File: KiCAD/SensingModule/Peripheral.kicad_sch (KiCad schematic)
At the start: 8 parts, among them J3 TERMISTOR, U10 BME280, U5 MB85RS2MT, U6 MB85RS2MT, U7 MB85RS2MT, U8 MB85RS2MT, U9 BNO055

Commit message: 配線作業終了、確認お願いします
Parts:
- J3: footprint TSRP_Connector_Hirose:DF51-2P-2DS -> TSRP_Connector:DF1B-2S-2.5R
- U9: footprint Akizuki_BNO055_Module:BNO055 -> TSRP_IC:AE-BNO055-BO
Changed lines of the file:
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@@
 			)
 		)
-		(property "Footprint" "Akizuki_BNO055_Module:BNO055"
+		(property "Footprint" "TSRP_IC:AE-BNO055-BO"
 			(at 179.07 41.91 0)
 			(effects
@@
 			)
 		)
-		(property "Footprint" "TSRP_Connector_Hirose:DF51-2P-2DS"
+		(property "Footprint" "TSRP_Connector:DF1B-2S-2.5R"
 			(at 105.41 46.99 0)
 			(effects

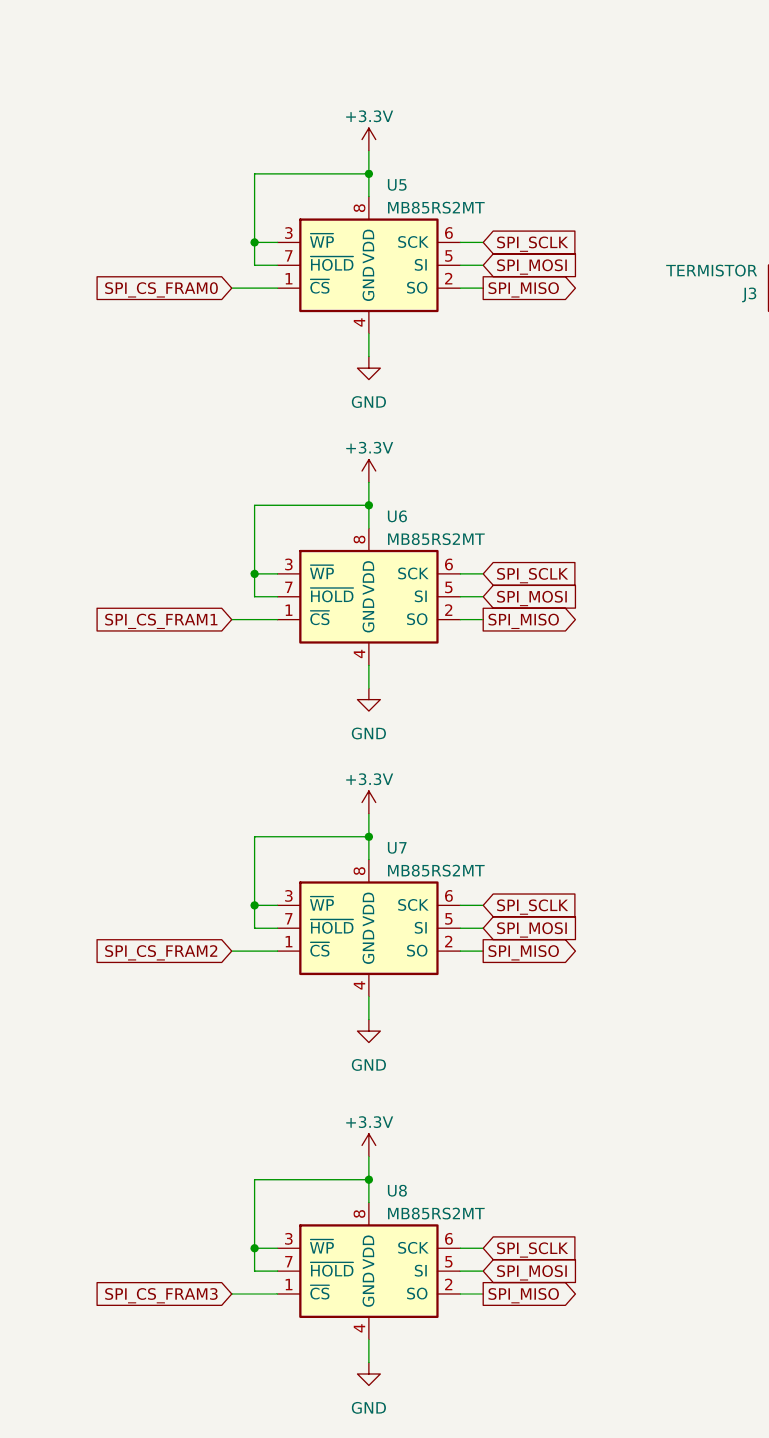
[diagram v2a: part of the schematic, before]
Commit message: Sensingの配線作業終わり、確認お願いします。
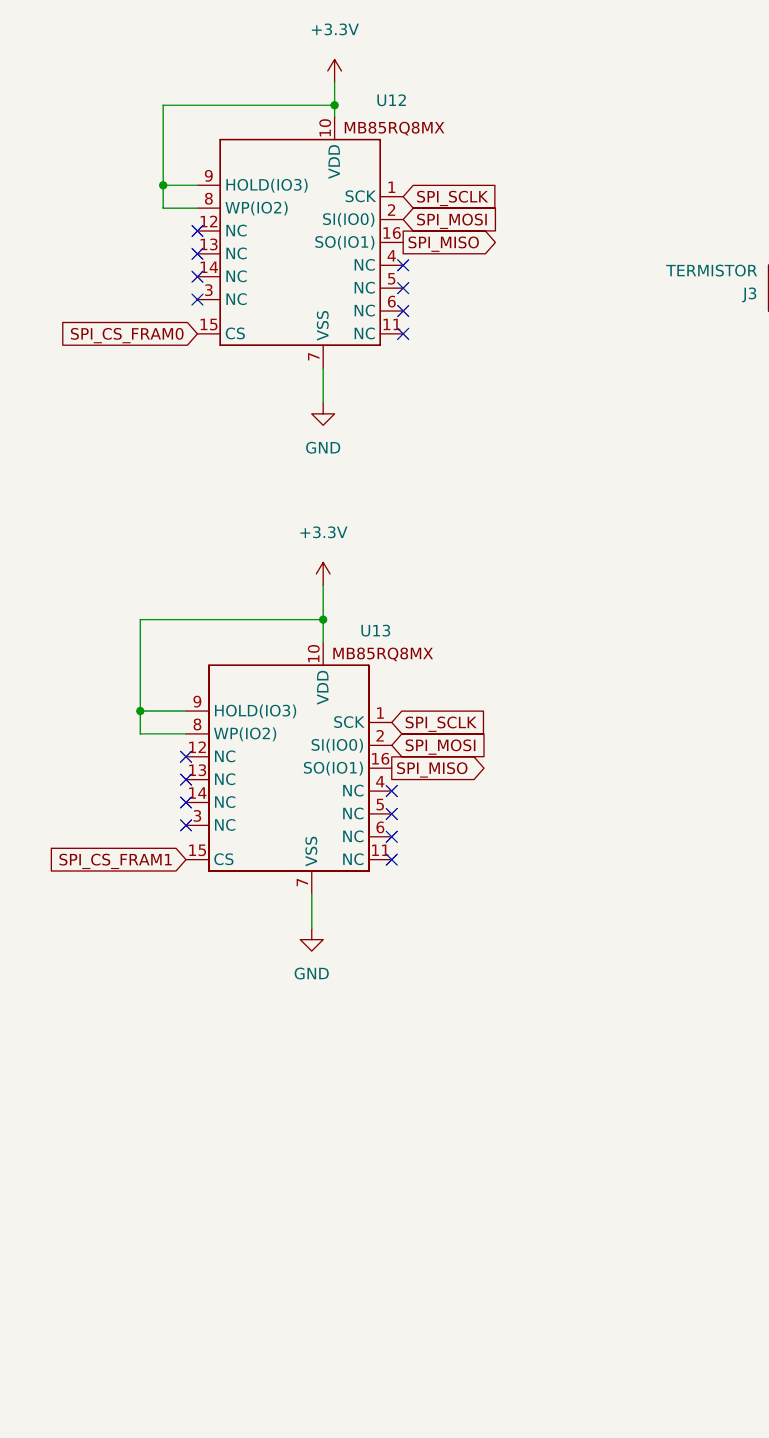
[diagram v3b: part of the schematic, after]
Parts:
- removed U5, U6, U7, U8: MB85RS2MT, Package_DIP:DIP-8_W7.62mm, symbol Memory_NVRAM:MB85RS2MT
- added U12, U13: ~, MB85RQ8MX:MB85RQ8MX, symbol MB85RQ8MX_sym:MB85RQMX
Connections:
- net +3.3V: now also U12.10 (VDD), U12.8 (WP(IO2)), U12.9 (HOLD(IO3)), U13.10 (VDD), U13.8 (WP(IO2)), U13.9 (HOLD(IO3))
- net GND: now also U12.7 (VSS), U13.7 (VSS)
- net SPI_CS_FRAM0: now also U12.15 (CS)
- net SPI_CS_FRAM1: now also U13.15 (CS)
- net SPI_MISO: now also U12.16 (SO(IO1)), U13.16 (SO(IO1))
- net SPI_MOSI: now also U12.2 (SI(IO0)), U13.2 (SI(IO0))
- net SPI_SCLK: now also U12.1 (SCK), U13.1 (SCK)
- no-connect marks 3 -> 19

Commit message: 配線確認お願いします
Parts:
- added U14: ~, Package_SO:SOIC-16W_7.5x10.3mm_P1.27mm, symbol MB85RQ8MX_sym:MB85RQMX
- U12, U13: footprint MB85RQ8MX:MB85RQ8MX -> Package_SO:SOIC-16W_7.5x10.3mm_P1.27mm
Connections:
- net +3.3V: now also U14.10 (VDD), U14.8 (WP(IO2)), U14.9 (HOLD(IO3))
- net GND: now also U14.7 (VSS)
- net SPI_MISO: now also U14.16 (SO(IO1))
- net SPI_MOSI: now also U14.2 (SI(IO0))
- net SPI_SCLK: now also U14.1 (SCK)
- new net SPI_CS_FRAM2: U14.15 (CS)
- no-connect marks 19 -> 27

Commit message: 簡単な警告を修正
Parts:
- J3: footprint TSRP_Connector:DF1B-2S-2.5R -> TSRP_Connector_Hirose:DF1B-2S-2.5R
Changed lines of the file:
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@@
 			)
 		)
-		(property "Footprint" "TSRP_Connector:DF1B-2S-2.5R"
+		(property "Footprint" "TSRP_Connector_Hirose:DF1B-2S-2.5R"
 			(at 105.41 46.99 0)
 			(effects

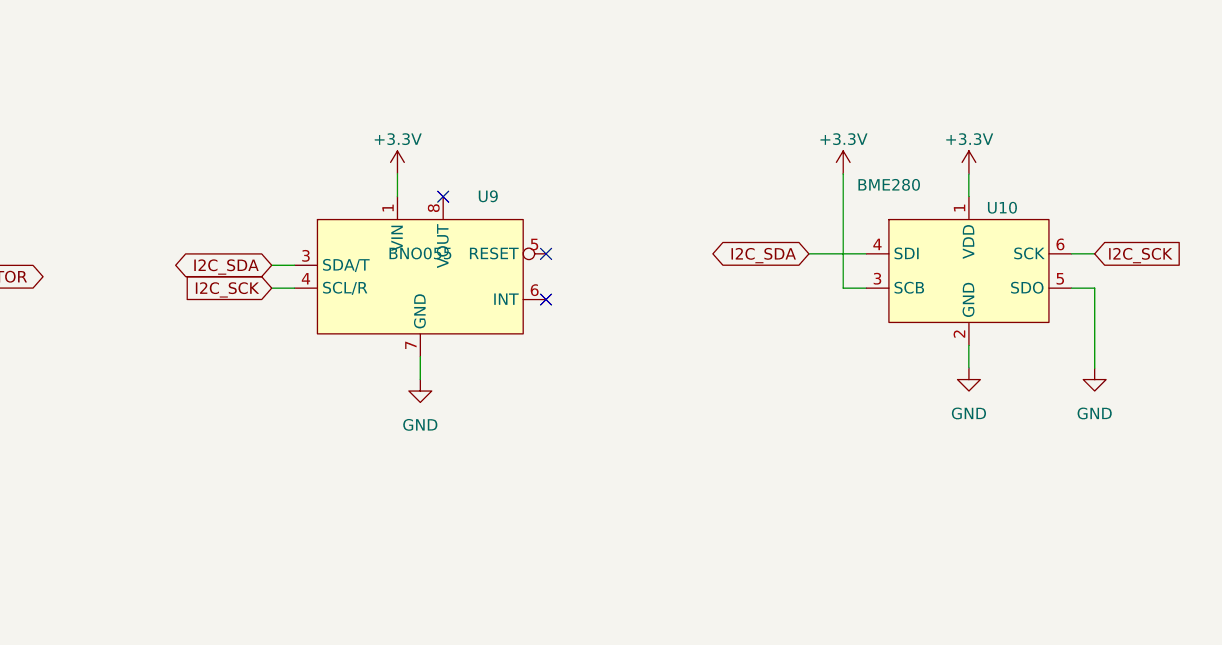
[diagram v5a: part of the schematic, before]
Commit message: BNO055のシンボルを変更．
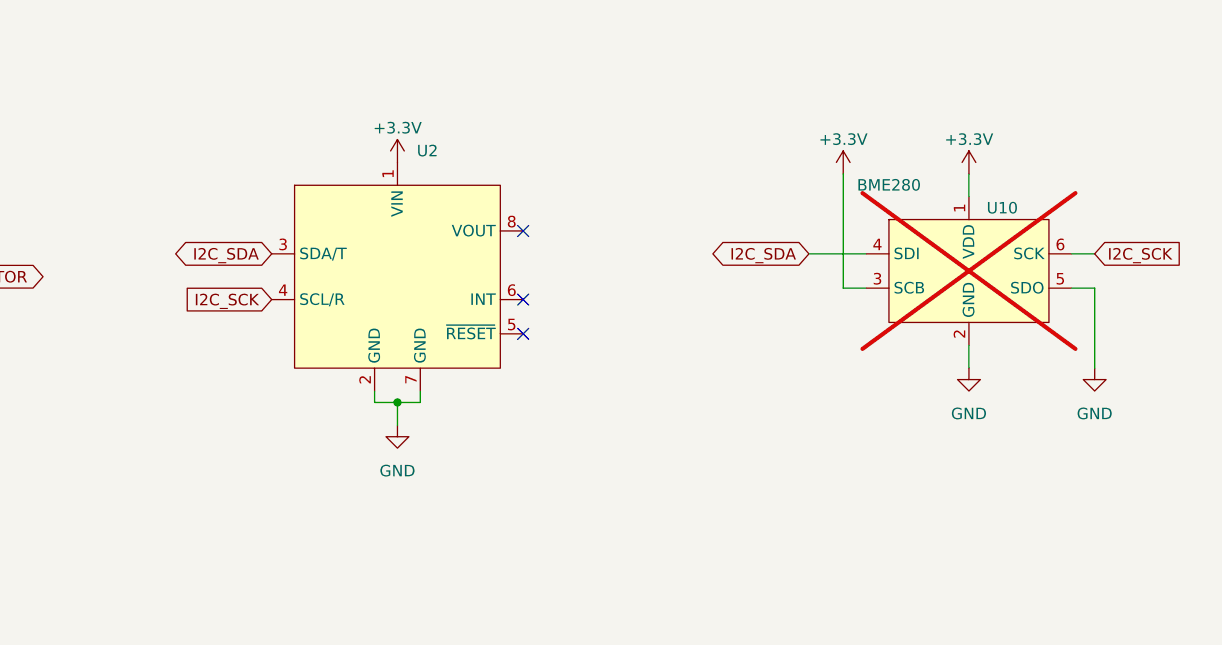
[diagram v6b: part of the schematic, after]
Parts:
- removed U9: BNO055, TSRP_IC:AE-BNO055-BO, symbol Akizuki_BNO055_Module:BNO055
- added U2: ~, TSRP_IC:AE-BNO055-BO, symbol TSRP_IC:AE-BNO055-BO
- U10: now not fitted; now left out of the parts list
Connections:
- net +3.3V: now also U2.1 (VIN)
- net GND: now also U2.2 (GND), U2.7 (GND)
- net I2C_SCK: now also U2.4 (SCL/R)
- net I2C_SDA: now also U2.3 (SDA/T)

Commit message: 最終確認終わり
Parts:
- J3: value TERMISTOR -> DF51-2P-2DS; footprint TSRP_Connector_Hirose:DF1B-2S-2.5R -> TSRP_Connector_Hirose:DF51-2P-2DS
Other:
- note added: "THERMISTOR"
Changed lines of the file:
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@@
 	(generator_version "9.0")
 	(paper "A4")
+	(text "THERMISTOR"
+		(exclude_from_sim no)
+		(at 105.156 40.386 0)
+		(effects
+			(font
+				(size 1.27 1.27)
+			)
+		)
+	)
 	(junction
 		(at 55.88 25.4)
@@
 			)
 		)
-		(property "Value" "TERMISTOR"
+		(property "Value" "DF51-2P-2DS"
 			(at 102.87 43.815 0)
 			(effects
@@
 			)
 		)
-		(property "Footprint" "TSRP_Connector_Hirose:DF1B-2S-2.5R"
+		(property "Footprint" "TSRP_Connector_Hirose:DF51-2P-2DS"
 			(at 105.41 46.99 0)
 			(effects

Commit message: きれいに配線できるようになった．
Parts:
- removed U10: BME280, Akizuki_BME280_Module:BME280, symbol Akizuki_BME280_Module:BME280
- removed U12, U13: ~, Package_SO:SOIC-16W_7.5x10.3mm_P1.27mm, symbol MB85RQ8MX_sym:MB85RQMX
- added C14, C15, C16, C17: 0.1uF, Capacitor_SMD:C_0603_1608Metric_Pad1.08x0.95mm_HandSolder, symbol Device:C
- added J4: DF51A-4P-2DS, TSRP_Connector_Hirose:DF51A-4P-2DS, symbol Connector_Generic:Conn_01x04
- added U5, U6, U7: MB85RQ8MX, Package_SO:SOIC-16W_7.5x10.3mm_P1.27mm, symbol TSRP_IC:MB85RQ8MX
- U14: now not fitted; now left out of the parts list
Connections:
- net +3.3V: now also C14.1, C15.1, C16.1, C17.1, J4.2 (Pin_2), U5.1 (~{HOLD}(IO3)), U5.2 (VDD), U5.9 (~{WP}(IO2)), U6.1 (~{HOLD}(IO3)), U6.2 (VDD), U6.9 (~{WP}(IO2)), U7.1 (~{HOLD}(IO3)), U7.2 (VDD), U7.9 (~{WP}(IO2))
- net GND: now also C14.2, C15.2, C16.2, C17.2, J4.1 (Pin_1), U5.10 (VSS), U6.10 (VSS), U7.10 (VSS)
- net I2C_SCK: now also J4.4 (Pin_4)
- net I2C_SDA: now also J4.3 (Pin_3)
- net SPI_MISO: now also U5.8 (SO(IO1)), U6.8 (SO(IO1)), U7.8 (SO(IO1))
- net SPI_MOSI: now also U5.15 (SI(IO0)), U6.15 (SI(IO0)), U7.15 (SI(IO0))
- net SPI_SCLK: now also U5.16 (SCK), U6.16 (SCK), U7.16 (SCK)
- new net SPI_~{CS}_FeRAM0: U5.7 (~{CS})
- new net SPI_~{CS}_FeRAM1: U6.7 (~{CS})
- new net SPI_~{CS}_FeRAM2: U7.7 (~{CS})
- no-connect marks 27 -> 11
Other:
- moved on the sheet: J3, R15, U2
